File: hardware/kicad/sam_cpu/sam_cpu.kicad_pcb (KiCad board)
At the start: 2 copper layers, 142 x 231.8 mm, 465 parts, among them J1 J1 SWITCH COLUMNS, J10 J10 SPEAKERS, J11 J11 POWER, J12 J12 SWITCH ROWS, J13 J13 DEDICATED, J17 EXT 5V, J18 J18 GI DIMMER, J19 USB-C (to Pi), J2 J2 DEDICATED, J20 SWD, J21 Raspberry Pi 40-pin, J22 J22 STEREO, J23 EXT 12V, J24 J24 SUBWOOFER, J25 J25 HUB75 PANEL A, J26 J26 HUB75 PANEL B, J3 J3 DEDICATED, J5 J5 DMD, J6 J6 SWITCH ROWS, J9 J9 IO BUS, Q1 AO3401A, Q11 MMBT3904, Q12 MMBT3904, Q13 MMBT3904, Q14 MMBT3904, Q15 MMBT3904, Q16 MMBT3904, Q17 MMBT3904, Q18 MMBT3904, Q2 AO3401A, Q3 2N7002, Q4 2N7002, SW1 RESET, SW2 BOOTSEL, SW3 DIP x8, U1 LTC4412, U10 LM339, U11 LM339, U14 74HC165, U15 74HC165, U16 74HC165, U17 74HC165, U18 74HC165, U19 74HC165, U2 LTC4412, U20 74HC595, U21 74HCT245, U22 PCM5102A, U23 TDA7297, U24 TDA7297, U25 DS3231MZ, U26 OPA1678, U27 74AHCT245, U28 74AHCT245, U29 74AHCT245, U3 NCP1117-3.3, U30 74HC165, U31 74HC595, U4 RP2354B, U5 TPS3808G33, U6 SN74LVC8T245, U7 74AHCT541, U8 LM339, U9 LM339, Y1 12MHz

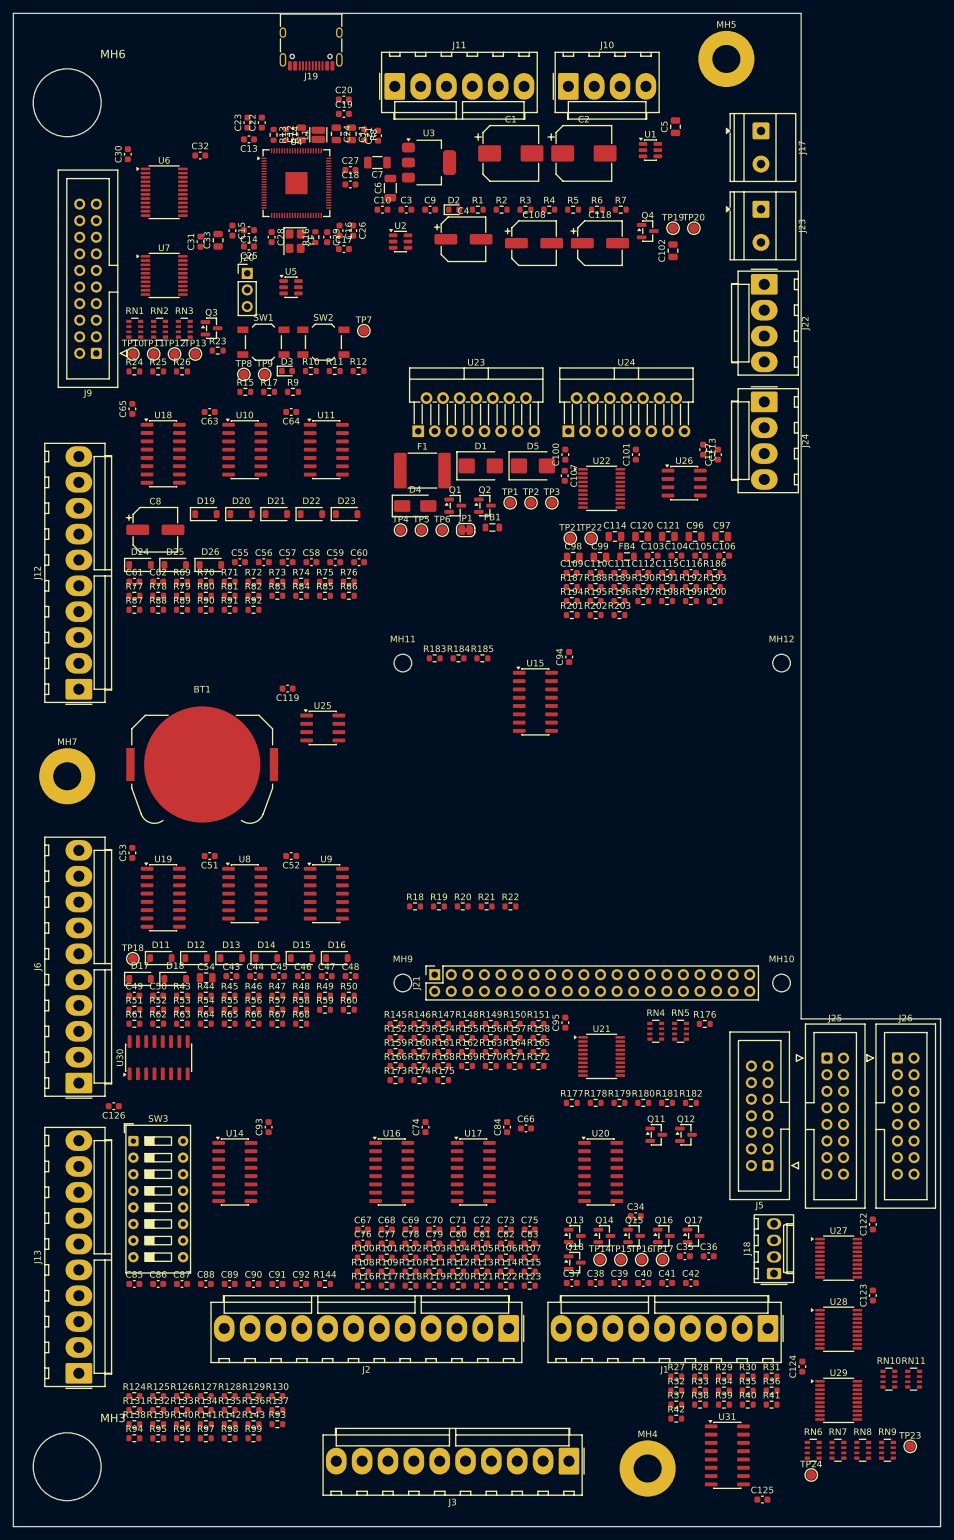
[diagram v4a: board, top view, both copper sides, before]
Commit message: Layout step 1: net classes, rules, hand-routed RP2354B regulator, GND zones
JLCPCB 2-layer rules (0.2 mm tracks, 0.15 mm clearance, 0.6/0.3 vias),
Power / Power_HI / Speaker net classes, core regulator routed on the top
layer per the RP2350 hardware guide and locked, GND zones on both layers.
tools/changes/c06_route_import.py imports the autorouted session next.

Co-Authored-By: Claude Opus 5.5 (1M context) <noreply@anthropic.com>
Claude-Session: https://claude.ai/code/session_01ExuDVoDDDHhVWjb8EwVzYb
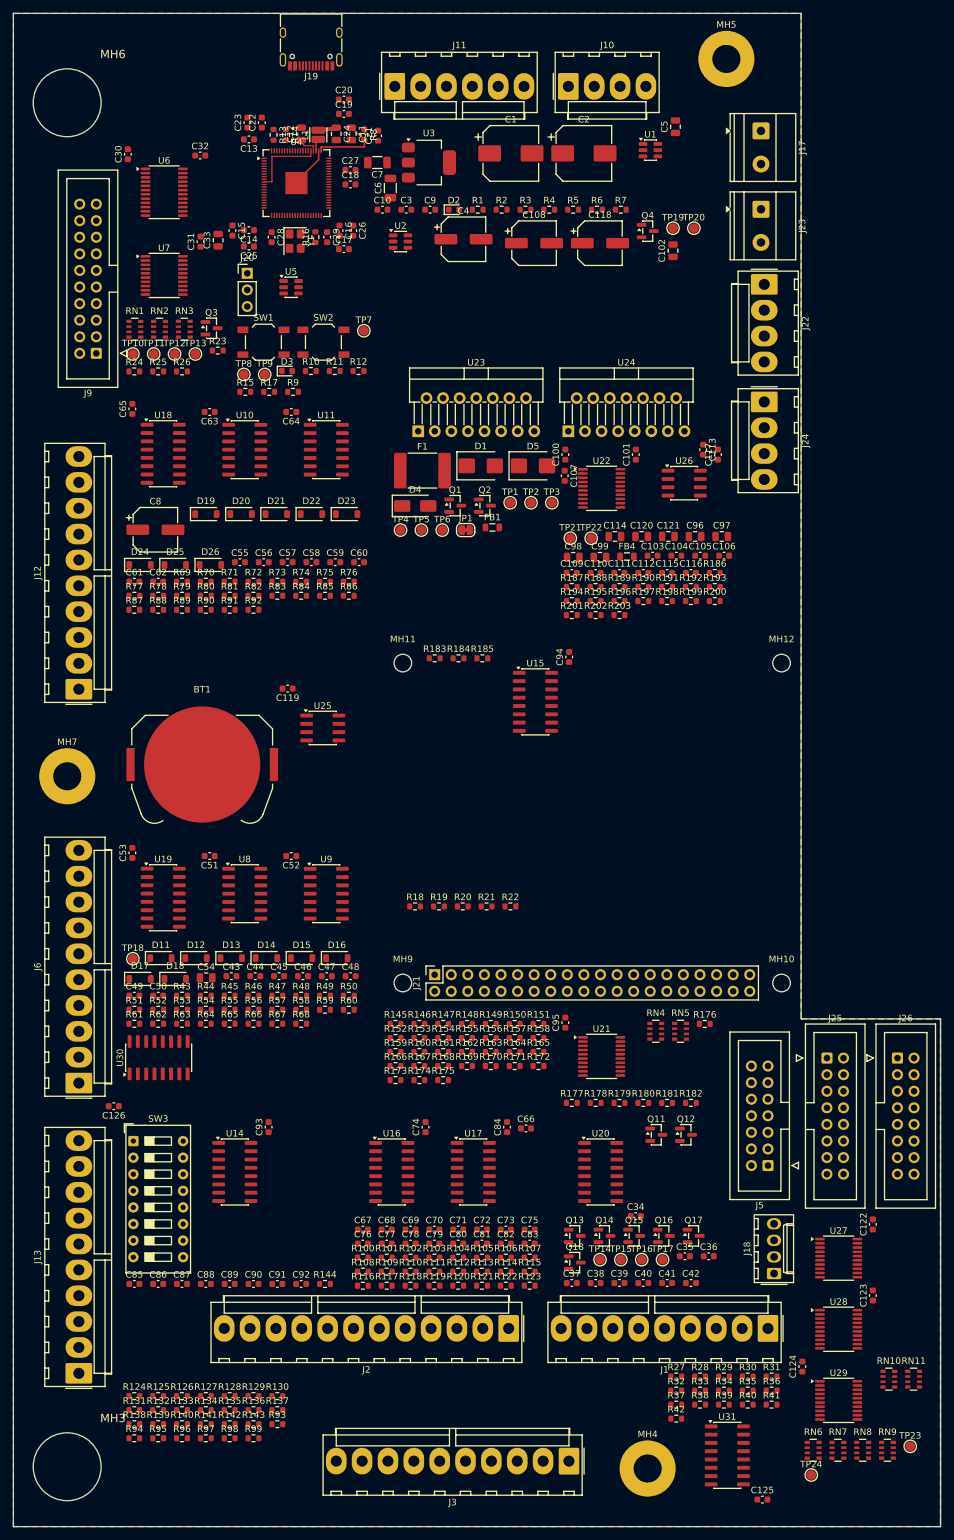
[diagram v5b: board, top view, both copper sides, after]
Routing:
- net +1V1: track 0.00 -> 14.7 mm
- net Net-(U4-VREG_AVDD): track 0.00 -> 11.0 mm
- net GND: track 0.00 -> 4.25 mm
- net +3V3: track 0.00 -> 2.63 mm
- net Net-(U4-VREG_LX): track 0.00 -> 1.75 mm
- added copper zone on B.Cu, net GND
- added copper zone on F.Cu, net GND
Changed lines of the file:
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@@
+		)
+	)
+	(segment
+		(start 74.55 50.25)
+		(end 74.3 49.9)
+		(width 0.2)
+		(locked yes)
+		(layer "F.Cu")
+		(net "+3V3")
+	)
+	(segment
+		(start 75.95 51.05)
+		(end 75.95 50.25)
+		(width 0.2)
+		(locked yes)
+		(layer "F.Cu")
+		(net "+3V3")
+	)
+	(segment
+		(start 75.95 50.25)
+		(end 74.55 50.25)
+		(width 0.2)
+		(locked yes)
+		(layer "F.Cu")
+		(net "+3V3")
+	)
+	(segment
+		(start 76.75 51.05)
+		(end 76.75 52.4)
+		(width 0.25)
+		(locked yes)
+		(layer "F.Cu")
+		(net "GND")
+	)
+	(segment
+		(start 76.75 52.4)
+		(end 74.7 54.45)
+		(width 0.25)
+		(locked yes)
+		(layer "F.Cu")
+		(net "GND")
+	)
+	(segment
+		(start 75.55 51.9)
+		(end 69.6 51.9)
+		(width 0.2)
+		(locked yes)
+		(layer "F.Cu")
+		(net "+1V1")
+	)
+	(segment
+		(start 69.6 55.8)
+		(end 68.4 55.8)
+		(width 0.2)
+		(locked yes)
+		(layer "F.Cu")
+		(net "+1V1")
+	)
+	(segment
+		(start 75.55 51.05)
+		(end 75.55 51.9)
+		(width 0.2)
+		(locked yes)
+		(layer "F.Cu")
+		(net "+1V1")
+	)
+	(segment
+		(start 76.7 47.9)
+		(end 79.45 47.6)
+		(width 0.6)
+		(locked yes)
+		(layer "F.Cu")
+		(net "+1V1")
+	)
+	(segment
+		(start 69.6 51.9)
+		(end 69.6 55.8)
+		(width 0.2)
+		(locked yes)
+		(layer "F.Cu")
+		(net "+1V1")
+	)
+	(segment
+		(start 82.8 48.45)
+		(end 81.75 47.5)
+		(width 0.25)
+		(locked yes)
+		(layer "F.Cu")
+		(net "Net-(U4-VREG_AVDD)")
+	)
+	(segment
+		(start 77.15 50.45)
+		(end 83.75 50.45)
+		(width 0.25)
+		(locked yes)
+		(layer "F.Cu")
+		(net "Net-(U4-VREG_AVDD)")
+	)
+	(segment
+		(start 83.75 49.42)
+		(end 82.8 48.45)
+		(width 0.25)
+		(locked yes)
+		(layer "F.Cu")
+		(net "Net-(U4-VREG_AVDD)")
+	)
+	(segment
+		(start 77.15 51.05)
+		(end 77.15 50.45)
+		(width 0.25)
+		(locked yes)
+		(layer "F.Cu")
+		(net "Net-(U4-VREG_AVDD)")
+	)
+	(segment
+		(start 83.75 50.45)
+		(end 83.75 49.42)
+		(width 0.25)
+		(locked yes)
+		(layer "F.Cu")
+		(net "Net-(U4-VREG_AVDD)")
+	)
+	(segment
+		(start 76.35 51.05)
+		(end 76.35 49.3)
+		(width 0.25)
+		(locked yes)
+		(layer "F.Cu")
+		(net "Net-(U4-VREG_LX)")
+	)
+	(zone
+		(net "GND")
+		(layer "F.Cu")
+		(name "GND_TOP")
+		(hatch edge 0.5)
+		(connect_pads
+			(clearance 0.25)
+		)
+		(min_thickness 0.2)
+		(fill
+			(thermal_gap 0.3)
+			(thermal_bridge_width 0.4)
+			(island_removal_mode 0)
+		)
+		(polygon
+			(pts
+				(xy 150.65 184) (xy 172 184) (xy 172 261.76) (xy 30 261.76) (xy 30 30) (xy 150.65 30)
+			)
+		)
+	)
+	(zone
+		(net "GND")
+		(layer "B.Cu")
+		(name "GND_BOT")
+		(hatch edge 0.5)
+		(connect_pads
+			(clearance 0.25)
+		)
+		(min_thickness 0.2)
+		(fill
+			(thermal_gap 0.3)
+			(thermal_bridge_width 0.4)
+			(island_removal_mode 0)
+		)
+		(polygon
+			(pts
+				(xy 150.65 184) (xy 172 184) (xy 172 261.76) (xy 30 261.76) (xy 30 30) (xy 150.65 30)
+			)
 		)
 	)

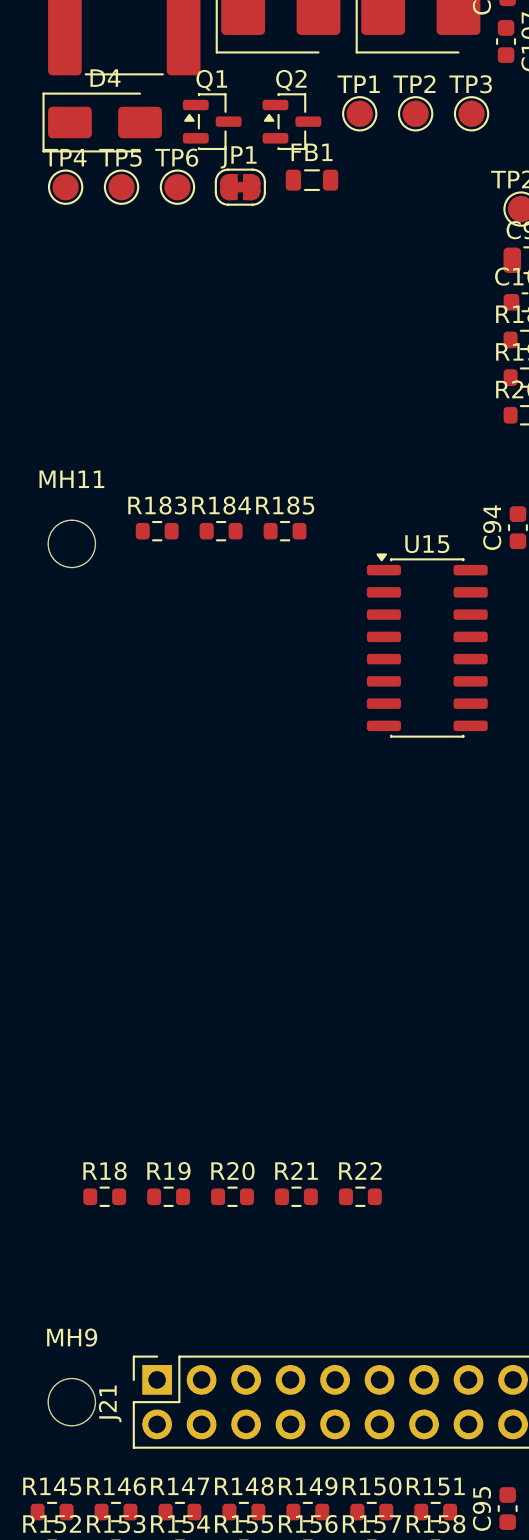
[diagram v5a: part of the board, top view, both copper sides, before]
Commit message: Layout: +5V trunk to the Pi header, thinner rail classes
Hand-routed 1.5 mm +5V trunk from the power-mux output under the Pi to
J21 pins 2/4 (locked); Power 0.25 mm, Power_5V 0.5 mm branches, so the
autorouter can reach every rail pin. Stale +5V pattern removed.

Co-Authored-By: Claude Opus 5.5 (1M context) <noreply@anthropic.com>
Claude-Session: https://claude.ai/code/session_01ExuDVoDDDHhVWjb8EwVzYb
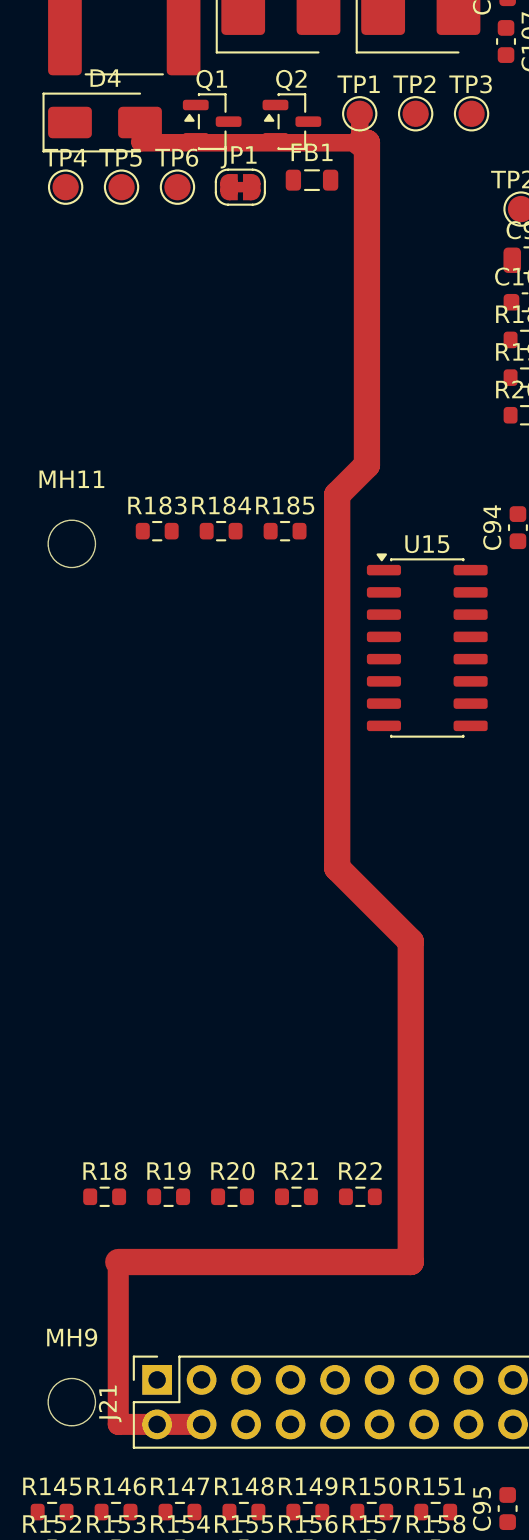
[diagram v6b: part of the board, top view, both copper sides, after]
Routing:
- net +5V: track 0.00 -> 112.8 mm
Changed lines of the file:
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@@
+	)
+	(segment
+		(start 75.95 50.25)
+		(end 74.55 50.25)
+		(width 0.2)
+		(locked yes)
+		(layer "F.Cu")
+		(net "+3V3")
+	)
+	(segment
+		(start 75.95 51.05)
+		(end 75.95 50.25)
+		(width 0.2)
+		(locked yes)
+		(layer "F.Cu")
+		(net "+3V3")
 	)
 	(segment
@@
 	)
 	(segment
-		(start 75.95 51.05)
-		(end 75.95 50.25)
-		(width 0.2)
-		(locked yes)
-		(layer "F.Cu")
-		(net "+3V3")
-	)
-	(segment
-		(start 75.95 50.25)
-		(end 74.55 50.25)
-		(width 0.2)
-		(locked yes)
-		(layer "F.Cu")
-		(net "+3V3")
-	)
-	(segment
 		(start 76.75 51.05)
 		(end 76.75 52.4)
@@
 	)
 	(segment
-		(start 75.55 51.9)
-		(end 69.6 51.9)
-		(width 0.2)
-		(locked yes)
-		(layer "F.Cu")
-		(net "+1V1")
+		(start 106.5 106.6)
+		(end 106.5 125)
+		(width 1.5)
+		(locked yes)
+		(layer "F.Cu")
+		(net "+5V")
+	)
+	(segment
+		(start 104.8 126.7)
+		(end 104.8 148)
+		(width 1.5)
+		(locked yes)
+		(layer "F.Cu")
+		(net "+5V")
+	)
+	(segment
+		(start 106.5 125)
+		(end 104.8 126.7)
+		(width 1.5)
+		(locked yes)
+		(layer "F.Cu")
+		(net "+5V")
+	)
+	(segment
+		(start 109 170.5)
+		(end 92.3 170.5)
+		(width 1.5)
+		(locked yes)
+		(layer "F.Cu")
+		(net "+5V")
+	)
+	(segment
+		(start 106.09 106.6)
+		(end 106.5 106.6)
+		(width 1.5)
+		(locked yes)
+		(layer "F.Cu")
+		(net "+5V")
+	)
+	(segment
+		(start 93.55 105.44)
+		(end 93.55 106.6)
+		(width 1)
+		(locked yes)
+		(layer "F.Cu")
+		(net "+5V")
+	)
+	(segment
+		(start 93.55 106.6)
+		(end 106.09 106.6)
+		(width 1)
+		(locked yes)
+		(layer "F.Cu")
+		(net "+5V")
+	)
+	(segment
+		(start 104.8 148)
+		(end 109 152.2)
+		(width 1.5)
+		(locked yes)
+		(layer "F.Cu")
+		(net "+5V")
+	)
+	(segment
+		(start 106.09 106.6)
+		(end 106.09 104.95)
+		(width 1)
+		(locked yes)
+		(layer "F.Cu")
+		(net "+5V")
+	)
+	(segment
+		(start 94.52 179.77)
+		(end 97.06 179.77)
+		(width 1.2)
+		(locked yes)
+		(layer "F.Cu")
+		(net "+5V")
+	)
+	(segment
+		(start 92.3 170.5)
+		(end 92.3 179.77)
+		(width 1.2)
+		(locked yes)
+		(layer "F.Cu")
+		(net "+5V")
+	)
+	(segment
+		(start 109 152.2)
+		(end 109 170.5)
+		(width 1.5)
+		(locked yes)
+		(layer "F.Cu")
+		(net "+5V")
+	)
+	(segment
+		(start 92.3 179.77)
+		(end 94.52 179.77)
+		(width 1.2)
+		(locked yes)
+		(layer "F.Cu")
+		(net "+5V")
 	)
 	(segment
 		(start 69.6 55.8)
 		(end 68.4 55.8)
-		(width 0.2)
-		(locked yes)
-		(layer "F.Cu")
-		(net "+1V1")
-	)
-	(segment
-		(start 75.55 51.05)
-		(end 75.55 51.9)
 		(width 0.2)
 		(locked yes)
@@
 	)
 	(segment
+		(start 75.55 51.9)
+		(end 69.6 51.9)
+		(width 0.2)
+		(locked yes)
+		(layer "F.Cu")
+		(net "+1V1")
+	)
+	(segment
 		(start 69.6 51.9)
 		(end 69.6 55.8)
@@
 	)
 	(segment
+		(start 75.55 51.05)
+		(end 75.55 51.9)
+		(width 0.2)
+		(locked yes)
+		(layer "F.Cu")
+		(net "+1V1")
+	)
+	(segment
+		(start 83.75 49.42)
+		(end 82.8 48.45)
+		(width 0.25)
+		(locked yes)
+		(layer "F.Cu")
+		(net "Net-(U4-VREG_AVDD)")
+	)
+	(segment
 		(start 82.8 48.45)
 		(end 81.75 47.5)
@@
 	)
 	(segment
+		(start 77.15 51.05)
+		(end 77.15 50.45)
+		(width 0.25)
+		(locked yes)
+		(layer "F.Cu")
+		(net "Net-(U4-VREG_AVDD)")
+	)
+	(segment
+		(start 83.75 50.45)
+		(end 83.75 49.42)
+		(width 0.25)
+		(locked yes)
+		(layer "F.Cu")
+		(net "Net-(U4-VREG_AVDD)")
+	)
+	(segment
 		(start 77.15 50.45)
 		(end 83.75 50.45)
 		(width 0.25)
 		(locked yes)
-		(layer "F.Cu")
-		(net "Net-(U4-VREG_AVDD)")
-	)
-	(segment
-		(start 83.75 49.42)
-		(end 82.8 48.45)
-		(width 0.25)
-		(locked yes)
-		(layer "F.Cu")
-		(net "Net-(U4-VREG_AVDD)")
-	)
-	(segment
-		(start 77.15 51.05)
-		(end 77.15 50.45)
-		(width 0.25)
-		(locked yes)
-		(layer "F.Cu")
-		(net "Net-(U4-VREG_AVDD)")
-	)
-	(segment
-		(start 83.75 50.45)
-		(end 83.75 49.42)
-		(width 0.25)
-		(locked yes)
